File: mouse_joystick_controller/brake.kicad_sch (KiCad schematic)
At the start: 4 parts, among them J1 Conn_TERM_HDR_01x02_Pin_3.5MM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, Q1 Q_NPN_ECB_BRT

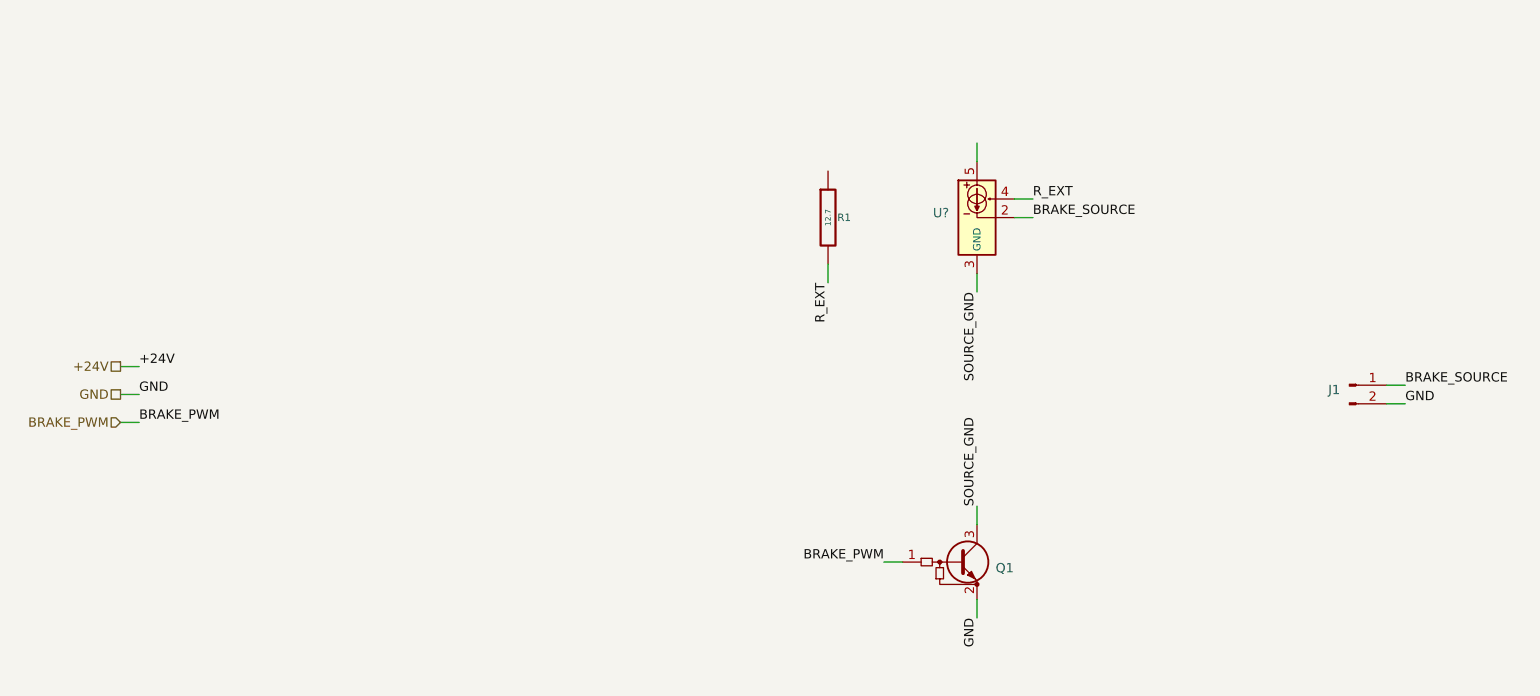
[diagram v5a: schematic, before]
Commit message: Change brake circuitry again
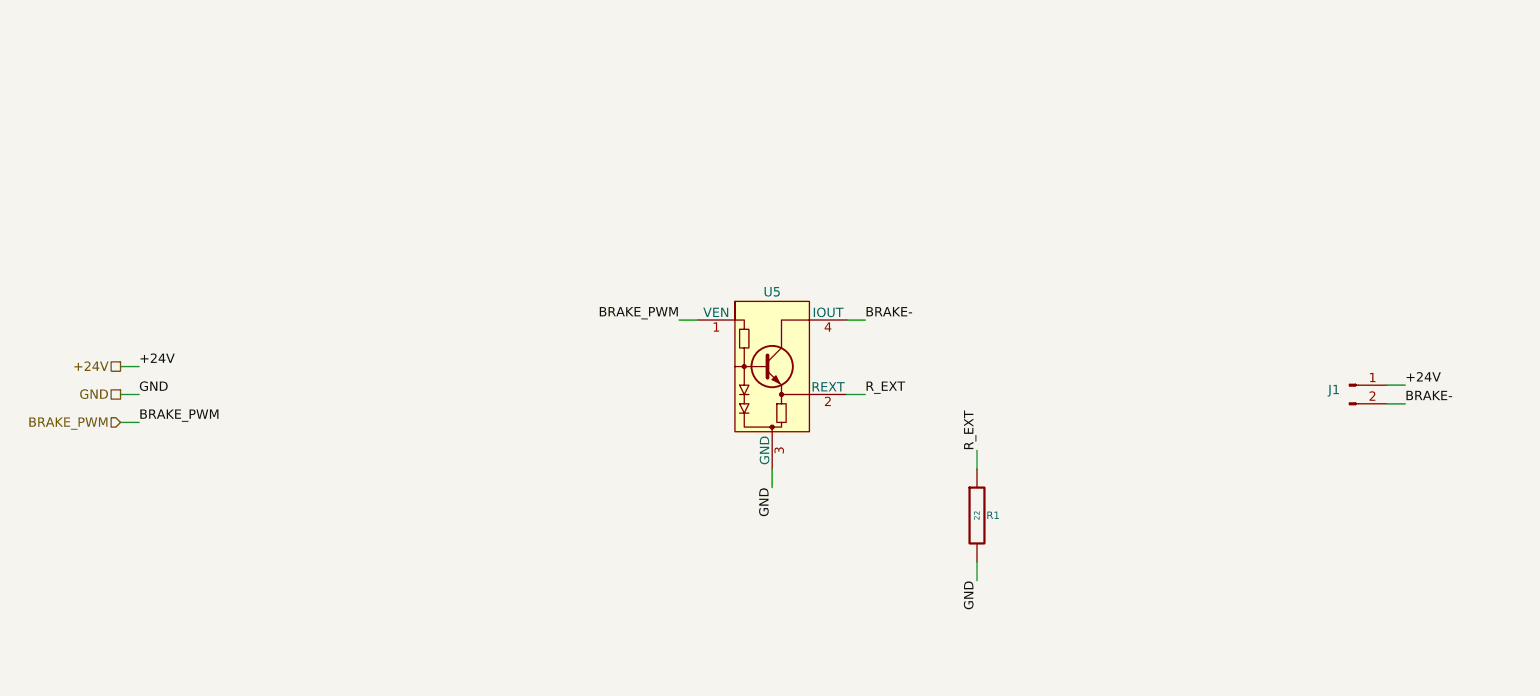
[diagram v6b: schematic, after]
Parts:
- removed Q1: Q_NPN_ECB_BRT, Janelia:XFDFN-3, symbol Janelia:Q_NPN_ECB_BRT_50V_100mA_PDTC124XMB,315
- removed R1: 12.7, Janelia:R_0402_1005Metric, symbol Janelia:R_12.7_0402
- removed U?: PSSI2021SAY, Janelia:SOT-353_SC-70-5, symbol Janelia:PSSI2021SAY
- added R1: 22, Janelia:R_0402_1005Metric, symbol Janelia:R_22_0402
- added U5: NCR421ZX, Janelia:SOT-223, symbol Janelia:NCR421ZX
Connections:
- net BRAKE_SOURCE is gone; now on net +24V: J1.1 (Pin_1)
- net BRAKE_PWM: now also U5.1 (VEN)
- net GND: now also R1.2, U5.3 (GND); no longer J1.2 (Pin_2)
- net R_EXT: now also R1.1, U5.2 (REXT)
- new net BRAKE-: J1.2 (Pin_2), U5.4 (IOUT)

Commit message: Add barrel jack connectors
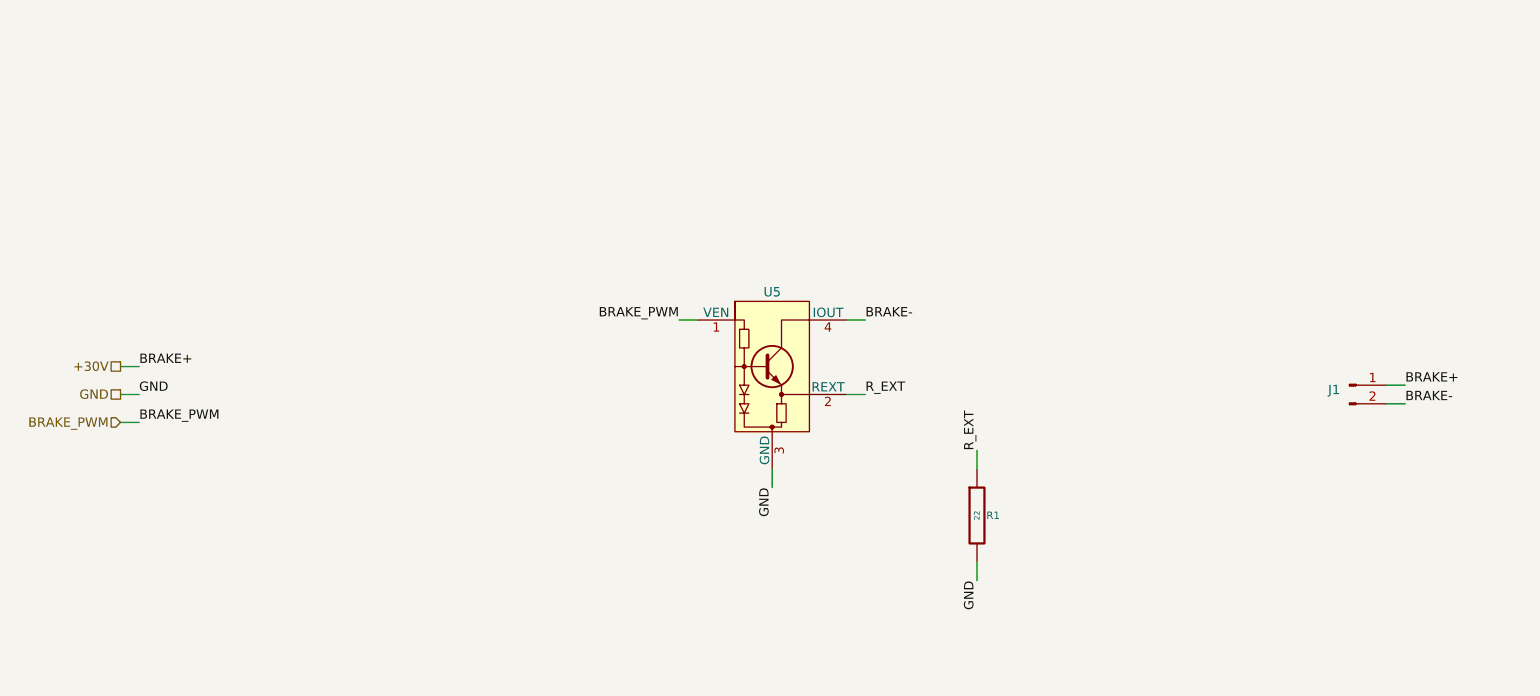
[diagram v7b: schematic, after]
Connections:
- net +24V renamed +30V
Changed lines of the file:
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@@
     (effects (font (size 1.27 1.27)) (justify right bottom))
   )
-  (label "+24V" (at 49.53 88.9 0) (fields_autoplaced)
+  (label "BRAKE+" (at 49.53 88.9 0) (fields_autoplaced)
     (effects (font (size 1.27 1.27)) (justify left bottom))
   )
@@
     (effects (font (size 1.27 1.27)) (justify left bottom))
   )
-  (label "+24V" (at 222.25 91.44 0) (fields_autoplaced)
+  (label "BRAKE+" (at 222.25 91.44 0) (fields_autoplaced)
     (effects (font (size 1.27 1.27)) (justify left bottom))
   )
@@
     (effects (font (size 1.27 1.27)) (justify right))
   )
-  (hierarchical_label "+24V" (shape passive) (at 46.99 88.9 180) (fields_autoplaced)
+  (hierarchical_label "+30V" (shape passive) (at 46.99 88.9 180) (fields_autoplaced)
     (effects (font (size 1.27 1.27)) (justify right))
   )

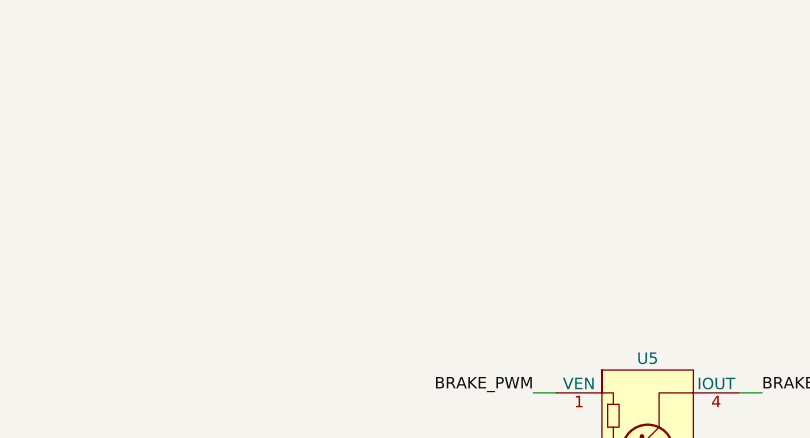
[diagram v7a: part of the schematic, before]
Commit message: Add DDS chip in audio sheet
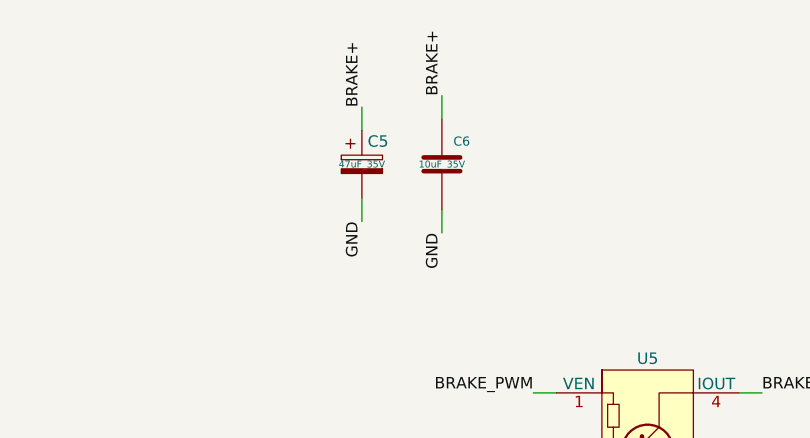
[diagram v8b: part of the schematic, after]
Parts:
- added C5: 47uF_35V, Janelia:CP_EIA-7343-43_Kemet-X, symbol Janelia:C_47uF_35V_2917_POL
- added C6: 10uF_35V, Janelia:C_0603_1608Metric, symbol Janelia:C_10uF_35V_0603
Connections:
- net +30V: now also C5.1, C6.1
- net GND: now also C5.2, C6.2
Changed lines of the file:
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@@
   (title_block
     (title "mouse_joystick_controller")
-    (date "2023-06-02")
+    (date "2023-06-06")
     (rev "2.0")
     (company "Howard Hughes Medical Institute")
   )
+  (wire (pts (xy 113.03 64.77) (xy 113.03 62.23))
+    (stroke (width 0) (type default))
+  )
   (wire (pts (xy 163.83 118.11) (xy 163.83 115.57))
     (stroke (width 0) (type default))
@@
     (stroke (width 0) (type default))
   )
+  (wire (pts (xy 104.14 63.5) (xy 104.14 60.96))
+    (stroke (width 0) (type default))
+  )
+  (wire (pts (xy 113.03 49.53) (xy 113.03 52.07))
+    (stroke (width 0) (type default))
+  )
   (wire (pts (xy 219.71 93.98) (xy 222.25 93.98))
     (stroke (width 0) (type default))
@@
     (stroke (width 0) (type default))
   )
+  (wire (pts (xy 104.14 50.8) (xy 104.14 53.34))
+    (stroke (width 0) (type default))
+  )
   (label "BRAKE_PWM" (at 123.19 82.55 180) (fields_autoplaced)
     (effects (font (size 1.27 1.27)) (justify right bottom))
   )
+  (label "GND" (at 113.03 64.77 270) (fields_autoplaced)
+    (effects (font (size 1.27 1.27)) (justify right bottom))
+  )
+  (label "BRAKE+" (at 113.03 49.53 90) (fields_autoplaced)
+    (effects (font (size 1.27 1.27)) (justify left bottom))
+  )
   (label "BRAKE+" (at 49.53 88.9 0) (fields_autoplaced)
     (effects (font (size 1.27 1.27)) (justify left bottom))
@@
     (effects (font (size 1.27 1.27)) (justify left bottom))
   )
+  (label "GND" (at 104.14 63.5 270) (fields_autoplaced)
+    (effects (font (size 1.27 1.27)) (justify right bottom))
+  )
   (label "BRAKE_PWM" (at 49.53 96.52 0) (fields_autoplaced)
     (effects (font (size 1.27 1.27)) (justify left bottom))
@@
   )
   (label "R_EXT" (at 148.59 92.71 0) (fields_autoplaced)
+    (effects (font (size 1.27 1.27)) (justify left bottom))
+  )
+  (label "BRAKE+" (at 104.14 50.8 90) (fields_autoplaced)
     (effects (font (size 1.27 1.27)) (justify left bottom))
   )
@@
     )
   )
+  (symbol (lib_id "Janelia:C_10uF_35V_0603") (at 113.03 57.15 0) (unit 1)
+    (in_bom yes) (on_board yes) (dnp no)
+    (property "Reference" "C6" (at 114.3 54.61 0)
+      (effects (font (size 1.016 1.016)) (justify left))
+    )
+    (property "Value" "10uF_35V" (at 113.03 57.15 0) (do_not_autoplace)
+      (effects (font (size 0.762 0.762)))
+    )
+    (property "Footprint" "Janelia:C_0603_1608Metric" (at 113.9952 60.96 0)
+      (effects (font (size 0.762 0.762)) hide)
+    )
+    (property "Datasheet" "" (at 113.03 57.15 0)
+      (effects (font (size 1.524 1.524)) hide)
+    )
+    (property "Description" "CAP CER 10UF 35V X5R" (at 120.65 46.99 0)
+      (effects (font (size 1.524 1.524)) hide)
+    )
+    (property "Package" "0603" (at 113.03 57.15 0)
+      (effects (font (size 1.524 1.524)) hide)
+    )
+    (property "Manufacturer" "Murata Electronics" (at 113.03 57.15 0)
+      (effects (font (size 1.524 1.524)) hide)
+    )
+    (property "Manufacturer Part Number" "GRM188R6YA106MA73D" (at 113.03 57.15 0)
+      (effects (font (size 1.524 1.524)) hide)
+    )
+    (property "Vendor" "Digi-Key" (at 113.03 57.15 0)
+      (effects (font (size 1.524 1.524)) hide)
+    )
+    (property "Vendor Part Number" "490-13248-1-ND" (at 113.03 57.15 0)
+      (effects (font (size 1.524 1.524)) hide)
+    )
+    (pin "1")
+    (pin "2")
+    (instances
+      (project "mouse_joystick_controller"
+        (path "/cc457ebc-4af6-4663-b19f-8cb38f061cb4/588c1a3c-052e-4e39-a8d9-29d79b9f5498"
+          (reference "C6") (unit 1)
+        )
+      )
+    )
+  )
   (symbol (lib_id "Janelia:Conn_TERM_HDR_01x02_Pin_3.5MM_Horizontal") (at 214.63 91.44 0) (unit 1)
     (in_bom yes) (on_board yes) (dnp no) (fields_autoplaced)
@@
         )
       )
+    )
+  )
+  (symbol (lib_id "Janelia:C_47uF_35V_2917_POL") (at 104.14 57.15 0) (unit 1)
+    (in_bom yes) (on_board yes) (dnp no) (fields_autoplaced)
+    (property "Reference" "C5" (at 104.775 54.61 0) (do_not_autoplace)
+      (effects (font (size 1.27 1.27)) (justify left))
+    )
+    (property "Value" "47uF_35V" (at 104.14 57.15 0) (do_not_autoplace)
+      (effects (font (size 0.762 0.762)))
+    )
+    (property "Footprint" "Janelia:CP_EIA-7343-43_Kemet-X" (at 104.14 43.18 0)
+      (effects (font (size 1.524 1.524)) hide)
+    )
+    (property "Datasheet" "" (at 104.394 55.372 0)
+      (effects (font (size 1.524 1.524)) hide)
+    )
+    (property "Vendor" "Digi-Key" (at 106.934 52.832 0)
+      (effects (font (size 1.524 1.524)) hide)
+    )
+    (property "Vendor Part Number" "399-11397-1-ND" (at 109.474 50.292 0)
+      (effects (font (size 1.524 1.524)) hide)
+    )
+    (property "Description" "CAP TANT 47UF 10% 35V" (at 112.014 47.752 0)
+      (effects (font (size 1.524 1.524)) hide)
+    )
+    (property "Package" "2917" (at 104.14 38.1 0)
+      (effects (font (size 1.27 1.27)) hide)
+    )
+    (property "Manufacturer" "KEMET" (at 104.14 45.72 0)
+      (effects (font (size 1.27 1.27)) hide)
+    )
+    (property "Manufacturer Part Number" "T498X476K035ATE500" (at 104.14 40.64 0)
+      (effects (font (size 1.27 1.27)) hide)
+    )
+    (pin "1")
+    (pin "2")
+    (instances
+      (project "mouse_joystick_controller"
+        (path "/cc457ebc-4af6-4663-b19f-8cb38f061cb4/588c1a3c-052e-4e39-a8d9-29d79b9f5498"
+          (reference "C5") (unit 1)
+        )
+      )
